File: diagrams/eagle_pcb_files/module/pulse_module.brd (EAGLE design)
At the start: 59.6 x 59.6 mm, 4 parts

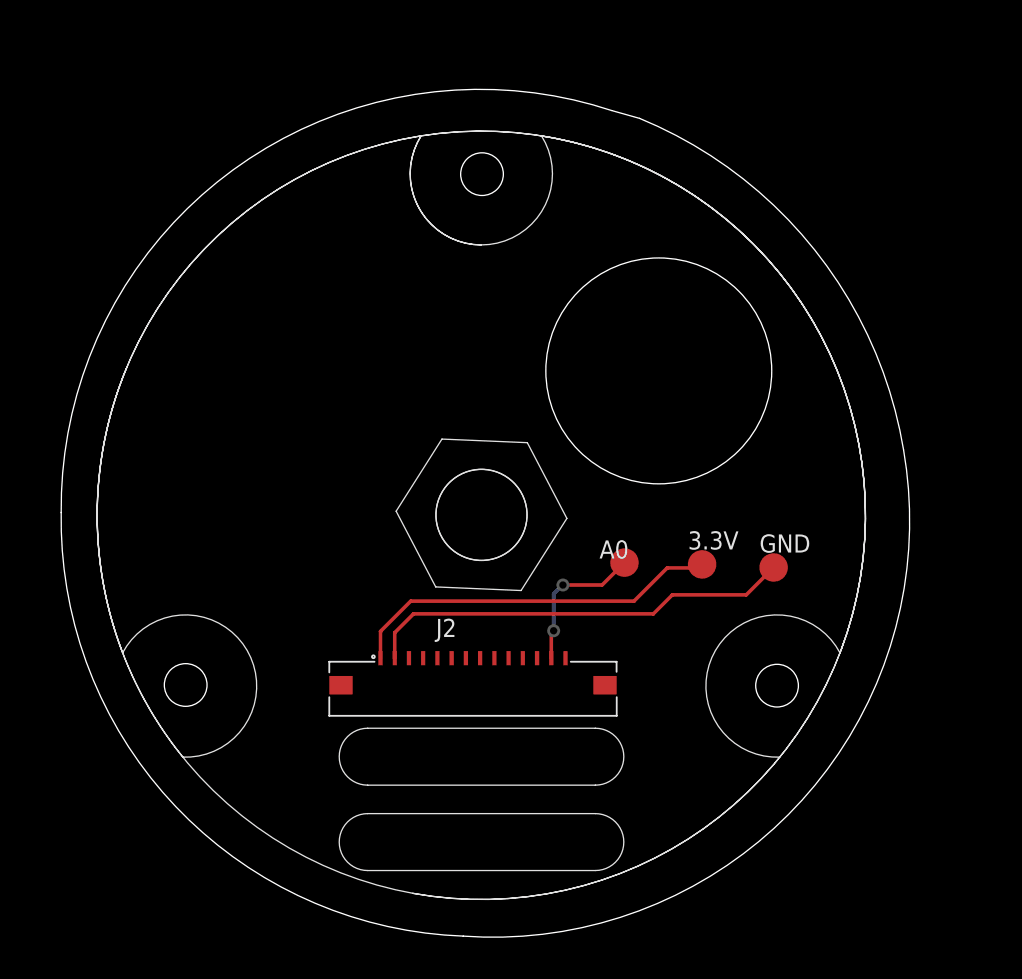
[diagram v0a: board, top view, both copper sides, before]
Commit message: GND plane, add 100nF cap
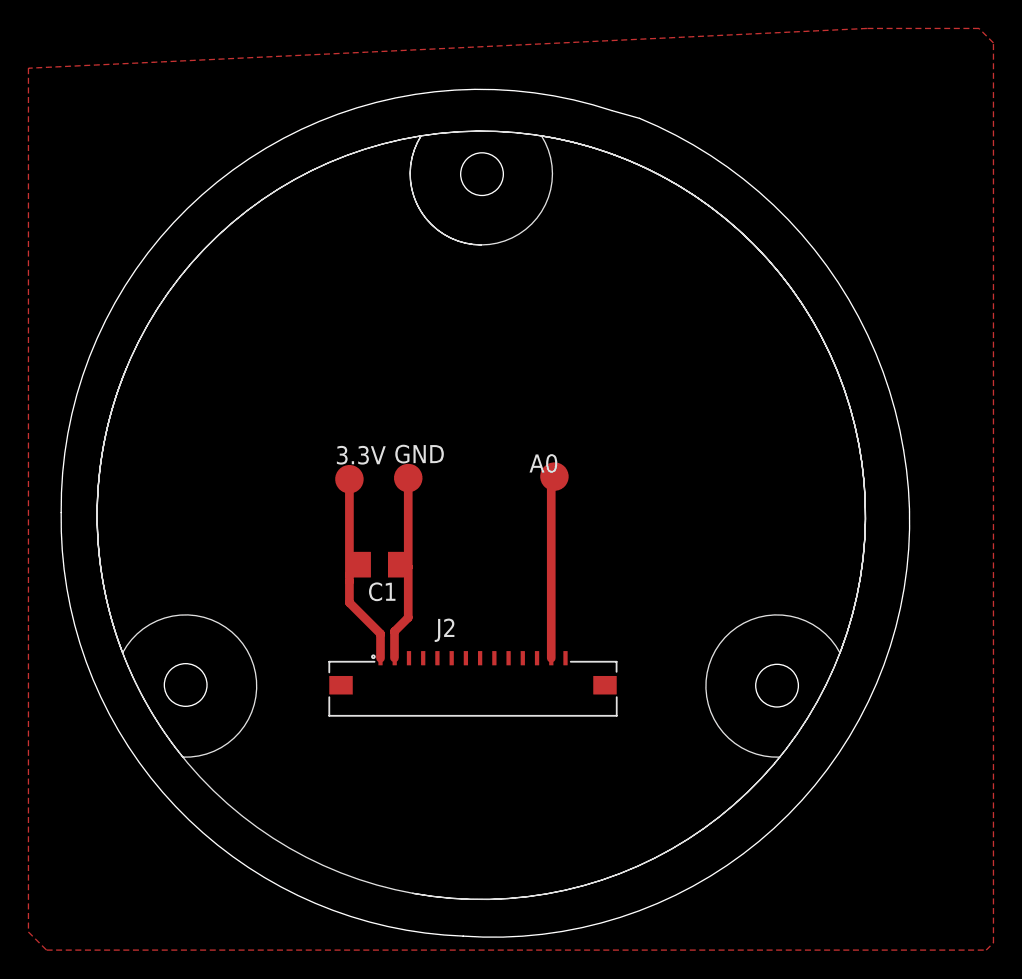
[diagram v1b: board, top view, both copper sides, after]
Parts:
- added C1: 100nF, rcl:C1206
- moved GND 26.4 mm to (50.8, 35.2)
- moved 3.3V 25.5 mm to (46.7, 35.1)
- moved A0 7.79 mm to (61.1, 35.3)
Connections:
- net 3.3V: now also C1.2
- net GND: now also C1.1
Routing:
- net GND: track 30.3 -> 13.8 mm
- net 3.3V: track 26.4 -> 14.8 mm
- net A0: track 10.5 -> 12.9 mm, vias 2 -> 0
- added copper zone on layer 1, net GND

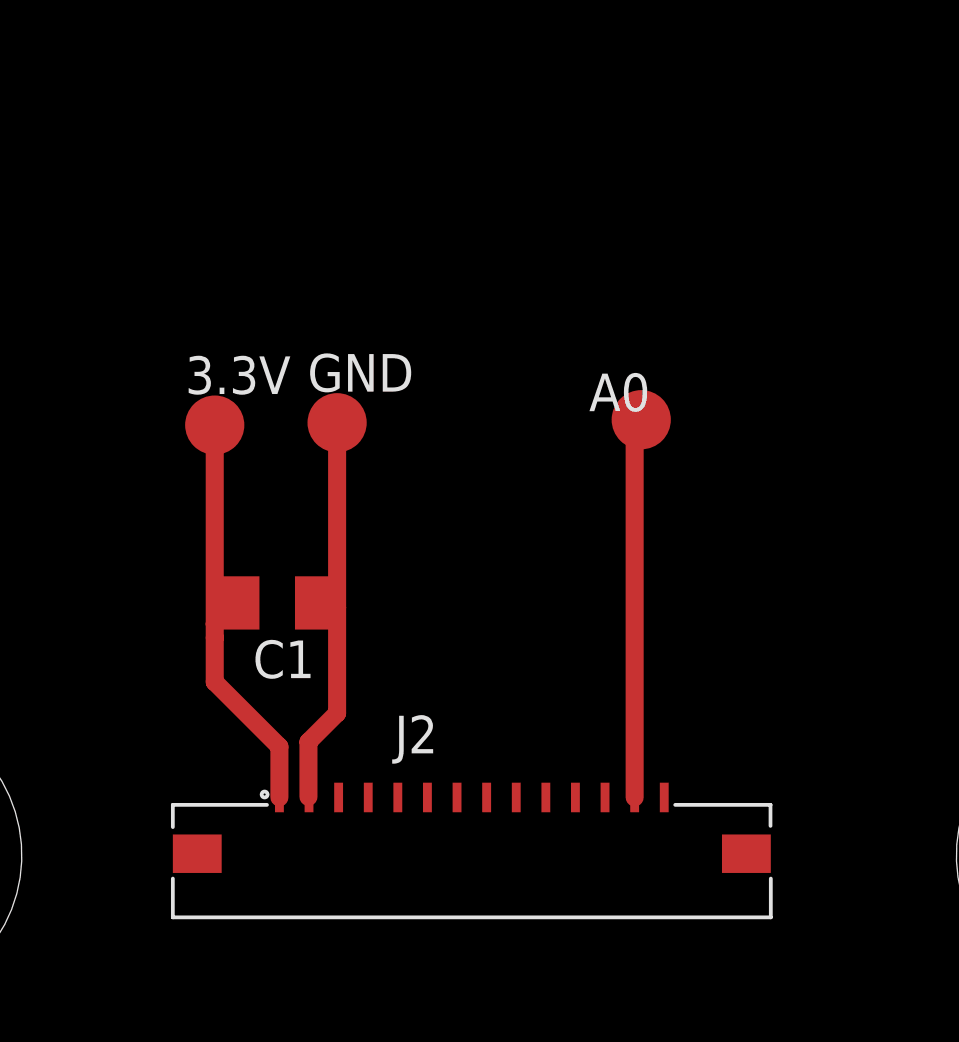
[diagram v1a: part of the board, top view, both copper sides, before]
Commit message: pulse module board with adc
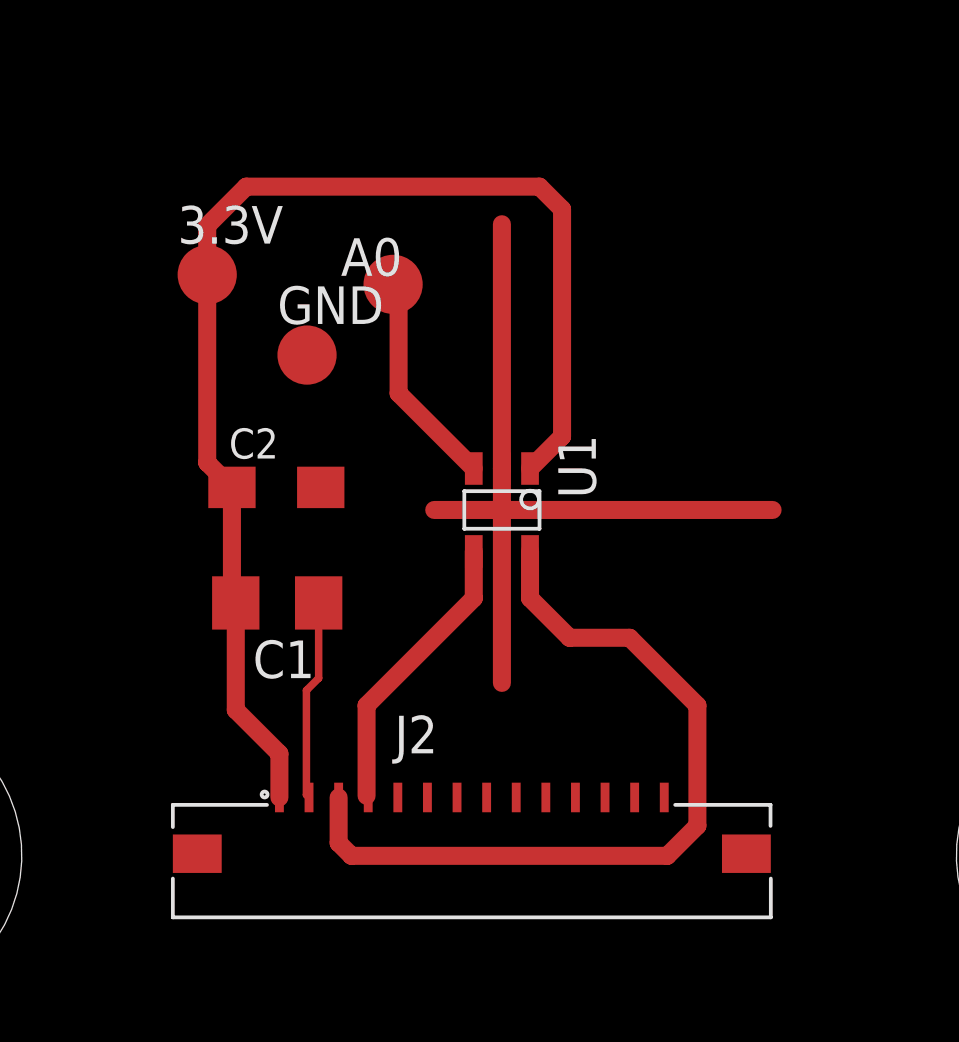
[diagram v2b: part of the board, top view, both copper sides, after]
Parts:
- added C2: 4.7uF, rcl:SMC_A
- added U1: MCP3021, Volks73-MicrochipTechnology:SOT-23-5
- moved A0 9.55 mm to (52.7, 39.9)
- moved 3.3V 5.09 mm to (46.4, 40.2)
- moved GND 2.50 mm to (49.8, 37.5)
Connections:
- removed net A0: A0.TP, J2.13
- removed net A1: J2.12
- removed net G1: J2.8
- removed net G2: J2.9
- removed net G3: J2.10
- removed net MISO: J2.7
- removed net MOSI: J2.6
- removed net SCK: J2.5
- removed net SS1: J2.11
- removed net VIN2: J2.14
- new net AIN: A0.TP, U1.3
- net 3.3V: now also C2.+, U1.1
- net GND: now also C2.-, U1.2
- net SCL: now also U1.5
- net SDA: now also U1.4
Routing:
- net 3.3V: track 14.8 -> 42.4 mm
- net SCL: track 0.00 -> 27.1 mm
- net GND: track 13.8 -> 33.7 mm
- net A0: track 12.9 -> 0.00 mm
- net SDA: track 0.00 -> 9.84 mm
- net AIN: track 0.00 -> 7.35 mm
